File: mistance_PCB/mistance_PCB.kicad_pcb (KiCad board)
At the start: 2 copper layers, 3 parts, among them U1 ESP32-WROOM-32E, U2 TPS61200DRC, U3 MCP73831-2-OT

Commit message: PCB update
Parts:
- added C1: 1uF, Capacitor_SMD:C_1210_3225Metric, F.Cu at (85.3, 44.9)
- added C2: 4.7uF, Capacitor_SMD:C_1210_3225Metric, F.Cu at (85.3, 49.1)
- added C3: 22uF, Capacitor_SMD:C_1210_3225Metric, F.Cu at (85.3, 53.4)
- added C4: 4.7uF, Capacitor_SMD:C_1210_3225Metric, F.Cu at (85.3, 57.6)
- added C5: 4.7uF, Capacitor_SMD:C_1210_3225Metric, F.Cu at (85.3, 61.9)
- added D1: D_Schottky, Diode_SMD:DIOM5226X220N, F.Cu at (93.3, 45.0)
- added J1: USB_B_Micro, Connector_USB:USB_Micro-B_Amphenol_10103594-0001LF_Horizontal, F.Cu at (82.7, 15.6)
- added Q1: Q_PMOS_DSG, SI2333DS-T1-E3:SOT95P237X112-3N, F.Cu at (88.5, 31.0)
- added R1: 2M, Resistor_SMD:R_1210_3225Metric, F.Cu at (95.5, 28.5)
- added R2: 180K, Resistor_SMD:R_1210_3225Metric, F.Cu at (95.5, 22.5)
- added R3: 10K, Resistor_SMD:R_0603_1608Metric, F.Cu at (77.0, 23.3)
- added R4: 10K, Resistor_SMD:R_0603_1608Metric, F.Cu at (82.5, 34.4)
- moved U2 26.8 mm to (104.0, 26.0)
- moved U3 2.44 mm to (78.5, 29.0), turned to 90 degrees
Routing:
- net GND: track 0.00 -> 12.6 mm
- net Net-(J1-D+): track 0.00 -> 0.65 mm

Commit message: PCB update
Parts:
- added BT1: Battery_Cell, Battery:BatteryHolder_MPD_BH-18650-PC2, F.Cu at (87.3, 81.1)
- added C6: 22uF, Capacitor_SMD:C_1210_3225Metric, F.Cu at (72.0, 57.5)
- added C7: 1uF, Capacitor_SMD:C_1210_3225Metric, F.Cu at (72.0, 61.8)
- added C8: 1uF, Capacitor_SMD:C_1210_3225Metric, F.Cu at (72.0, 66.0)
- added L1: 2.2uH, Inductor_SMD:L_1210_3225Metric, F.Cu at (64.6, 57.8)
- added R5: 10K, Resistor_SMD:R_0603_1608Metric, F.Cu at (76.9, 56.6)
- added U4: AMS1117-3.3, Package_TO_SOT_SMD:SOT-223-3_TabPin2, F.Cu at (72.4, 38.7)
- U3: footprint Package_TO_SOT_SMD:SOT-23-5 -> Package_TO_SOT_SMD:SOT95P280X145-5N
- moved R2 53.5 mm to (64.6, 66.2), turned to 0 degrees
- moved J1 50.1 mm to (88.4, 65.3), turned to 90 degrees
- moved R1 45.6 mm to (64.6, 62.0), turned to 0 degrees
- moved U2 41.5 mm to (70.1, 50.0)
- moved R3 25.5 mm to (80.2, 48.6), turned to 0 degrees
- moved Q1 22.5 mm to (75.7, 49.6), turned to 0 degrees
- moved C1 22.3 mm to (64.6, 36.6)
- moved C2 22.3 mm to (64.6, 40.8)
- moved C3 22.3 mm to (64.6, 45.1)
- moved C4 22.3 mm to (64.6, 49.3)
- moved C5 22.3 mm to (64.6, 53.6)
- moved U3 21.3 mm to (84.6, 49.5), turned to 0 degrees
- moved D1 20.7 mm to (72.7, 45.1)
- moved R4 16.9 mm to (80.2, 51.1), turned to 0 degrees
- moved U1 4.27 mm to (36.2, 43.2)
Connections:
- U1 pad 2: unconnected-(U1-VDD-Pad2) -> 3.3V OUT
- U1 pad 3: unconnected-(U1-EN-Pad3) -> Net-(U1-EN)
- U1 pad 34: unconnected-(U1-RXD0/IO3-Pad34) -> RX
- U1 pad 35: unconnected-(U1-TXD0/IO1-Pad35) -> TX
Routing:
- net GND: track 12.6 -> 164.4 mm, vias 0 -> 10
- net 5v OUT: track 0.00 -> 87.8 mm, vias 0 -> 3
- net Net-(BT1-+): track 0.00 -> 81.6 mm, vias 0 -> 1
- net 3.3V OUT: track 0.00 -> 72.1 mm, vias 0 -> 6
- net Net-(U1-EN): track 0.00 -> 69.7 mm, vias 0 -> 5
- net Net-(D1-A): track 0.00 -> 60.2 mm
- net Net-(Q1-D): track 0.00 -> 59.9 mm, vias 0 -> 3
- net Net-(U4-GND): track 0.00 -> 56.3 mm
- net Net-(U2-UVLO): track 0.00 -> 25.4 mm, vias 0 -> 2
- net Net-(U2-VAUX): track 0.00 -> 18.7 mm, vias 0 -> 2
- net Net-(U2-L): track 0.00 -> 13.0 mm, vias 0 -> 2
- net Net-(U3-PROG): track 0.00 -> 7.17 mm

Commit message: PCB update
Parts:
- added C10: 0.1uF, Capacitor_SMD:C_1210_3225Metric, F.Cu at (50.0, 45.8)
- added C11: 1uF, Capacitor_SMD:C_1210_3225Metric, F.Cu at (50.0, 50.0)
- added C9: 0.1uF, Capacitor_SMD:C_1210_3225Metric, F.Cu at (47.8, 64.8)
- added D2: PTVS5V0Z1USK, Diode_SMD:D_01005_0402Metric, F.Cu at (54.2, 44.5)
- added D3: PTVS5V0Z1USK, Diode_SMD:D_01005_0402Metric, F.Cu at (54.2, 46.1)
- added D4: PTVS5V0Z1USK, Diode_SMD:D_01005_0402Metric, F.Cu at (54.2, 47.8)
- added J2: USB_B_Micro, Connector_USB:USB_Micro-B_Amphenol_10103594-0001LF_Horizontal, F.Cu at (88.4, 42.7)
- added L2: 2.2uH, Inductor_SMD:L_1210_3225Metric, F.Cu at (53.4, 64.8)
- added PolarizedCapacitor1: 4.7uF, Capacitor_SMD:C_1210_3225Metric, F.Cu at (50.0, 54.2)
- added PolarizedCapacitor2: 4.7uF, Capacitor_SMD:C_1210_3225Metric, F.Cu at (50.0, 58.5)
- added R6: 22, Resistor_SMD:R_0603_1608Metric, F.Cu at (58.2, 64.0)
- added R7: 22, Resistor_SMD:R_0603_1608Metric, F.Cu at (58.2, 66.5)
- added R8: 4.7K, Resistor_SMD:R_0603_1608Metric, F.Cu at (54.9, 49.8)
- added U5: CP2104, Package_DFN_QFN:QFN-24-1EP_4x4mm_P0.5mm_EP2.6x2.6mm, F.Cu at (57.5, 57.9)
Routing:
- net GND: track 164.4 -> 262.9 mm, vias 10 -> 20
- net Net-(D2-K): track 0.00 -> 79.6 mm, vias 0 -> 6
- net Net-(D3-K): track 0.00 -> 77.0 mm, vias 0 -> 5
- net Net-(D4-K): track 0.00 -> 72.7 mm, vias 0 -> 2
- net 3.3v OUT CP2104: track 0.00 -> 34.6 mm, vias 0 -> 2
- net 3.3V OUT: track 72.1 -> 105.4 mm, vias 6 -> 8
- net USB 5V OUT: track 0.00 -> 29.7 mm, vias 0 -> 2
- net TX: track 0.00 -> 25.7 mm, vias 0 -> 4
- net Net-(U5-VPP): track 0.00 -> 25.5 mm, vias 0 -> 2
- net RX: track 0.00 -> 22.4 mm, vias 0 -> 4
- net Net-(U5-~{RST}): track 0.00 -> 20.6 mm, vias 0 -> 2
- net Net-(U5-D+): track 0.00 -> 11.6 mm
- net Net-(U5-D-): track 0.00 -> 7.75 mm
- net Net-(U1-EN): track 69.7 -> 72.2 mm
- net Net-(D1-A): track 60.2 -> 58.1 mm

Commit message: PCB update
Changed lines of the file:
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@@
 		)
 		(property "Value" "MCP73831-2-OT"
-			(at 13.4146 0.5394 0)
+			(at -0.0854 3.5394 0)
 			(layer "F.Fab")
 			(effects
@@
 		(tags "capacitor")
 		(property "Reference" "PolarizedCapacitor2"
-			(at -9.525 0 0)
+			(at -10.025 0 0)
 			(layer "F.SilkS")
 			(effects
@@
 		(tags "capacitor")
 		(property "Reference" "PolarizedCapacitor1"
-			(at -10.025 -0.25 0)
+			(at -10.025 0.75 0)
 			(layer "F.SilkS")
 			(effects

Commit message: PCB update
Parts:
- added C12: 0.1uF, Capacitor_SMD:C_1210_3225Metric, F.Cu at (13.1, 40.9)
- added C13: PESD0402-140, PESD0402-140:RESC1005X35N, F.Cu at (6.06, 58.0)
- added C14: PESD0402-140, PESD0402-140:RESC1005X35N, F.Cu at (6.06, 56.9)
- added C15: PESD0402-140, PESD0402-140:RESC1005X35N, F.Cu at (6.06, 55.7)
- added C16: PESD0402-140, PESD0402-140:RESC1005X35N, F.Cu at (89.5, 43.6)
- added C17: PESD0402-140, PESD0402-140:RESC1005X35N, F.Cu at (89.5, 45.8)
- added C18: 0.1uF, Capacitor_SMD:C_1210_3225Metric, F.Cu at (18.1, 68.5)
- added C19: 4.7uF, Capacitor_SMD:C_1210_3225Metric, F.Cu at (21.3, 68.5)
- added C20: 27pF, Capacitor_SMD:C_0603_1608Metric, F.Cu at (79.0, 16.0)
- added C21: 12pF, Capacitor_SMD:C_0402_1005Metric, F.Cu at (86.8, 64.7)
- added C22: 12pF, Capacitor_SMD:C_0402_1005Metric, F.Cu at (86.8, 66.6)
- added C23: 0.1uF, Capacitor_SMD:C_1210_3225Metric, F.Cu at (70.1, 61.6)
- added C24: 22uF, Capacitor_SMD:C_1210_3225Metric, F.Cu at (75.7, 36.1)
- added C25: 1uF, Capacitor_SMD:C_1210_3225Metric, F.Cu at (75.7, 40.3)
- added C26: 10uF, Capacitor_SMD:C_1210_3225Metric, F.Cu at (75.7, 44.6)
- added J3: GRPB052VWVN-RC, Varistor:SULLINS_GRPB052VWVN-RC, F.Cu at (14.1, 61.4)
- added J4: OLED, HTSW-104-20-TM-S:SAMTEC_HTSW-104-20-TM-S, F.Cu at (13.7, 71.1)
- added J5: SMA-J-P-X-ST-TH1, SMA-J-P-X-ST-TH1:SAMTEC_SMA-J-P-X-ST-TH1, F.Cu at (84.5, 16.0)
- added L4: WE-TPC_2811, WE-TPC_2811:WE-TPC_2811, F.Cu at (75.5, 16.0)
- added R10: 100R, Resistor_SMD:R_0603_1608Metric, F.Cu at (13.9, 55.3)
- added R11: 100R, Resistor_SMD:R_0603_1608Metric, F.Cu at (13.9, 53.8)
- added R12: 100R, Resistor_SMD:R_0603_1608Metric, F.Cu at (13.9, 52.3)
- added R13: 100R, Resistor_SMD:R_0603_1608Metric, F.Cu at (13.9, 50.8)
- added R14: 2.2K, Resistor_SMD:R_0603_1608Metric, F.Cu at (88.6, 56.2)
- added R15: 2.2K, Resistor_SMD:R_0603_1608Metric, F.Cu at (88.6, 58.7)
- added R9: 100K, Resistor_SMD:R_0603_1608Metric, F.Cu at (17.5, 47.6)
- added S1: SKRPABE010, Diode_SMD:SW_SKRPABE010, F.Cu at (13.3, 37.1)
- added U6: TPS3839DBZ, Package_TO_SOT_SMD:SOT-23, F.Cu at (13.0, 46.7)
- added U7: SX1278, Package_DFN_QFN:QFN-28-1EP_6x6mm_P0.65mm_EP4.8x4.8mm, F.Cu at (76.0, 22.0)
- added Y1: Crystal, Crystal:Crystal_SMD_2012-2Pin_2.0x1.2mm, F.Cu at (87.2, 69.0)
- C8: value 1uF -> PESD0402-140; footprint Capacitor_SMD:C_1210_3225Metric -> PESD0402-140:RESC1005X35N
- moved J2 93.9 mm to (16.5, 103.1), turned to 0 degrees
- moved J1 71.6 mm to (27.5, 103.0), turned to 0 degrees
- moved C8 66.3 mm to (6.06, 59.2), turned to 180 degrees
- moved R5 61.9 mm to (17.8, 38.2)
- moved C6 52.0 mm to (23.2, 39.5)
- moved C7 52.0 mm to (23.2, 43.8)
- moved U2 49.1 mm to (32.9, 82.0)
- moved U5 47.5 mm to (21.1, 88.2)
- moved D4 46.6 mm to (87.7, 80.2)
- moved D2 46.6 mm to (87.7, 76.8)
- moved D3 46.6 mm to (87.7, 78.5)
- moved Q1 44.4 mm to (42.2, 78.7)
- moved U4 42.7 mm to (35.5, 60.2)
- moved U3 40.3 mm to (56.7, 78.6)
- moved C9 36.4 mm to (70.1, 36.1)
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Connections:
- C8 pad 1: Net-(U1-EN) -> Net-(C8-Pad1)
- R5 pad 1: 3.3V OUT -> EN
- R5 pad 2: Net-(U1-EN) -> 3.3V OUT
- U1 pad 11: unconnected-(U1-IO26-Pad11) -> DIO0(IRQ)
- U1 pad 13: unconnected-(U1-IO14-Pad13) -> MTMS
- U1 pad 14: unconnected-(U1-IO12-Pad14) -> MTDI
- U1 pad 16: unconnected-(U1-IO13-Pad16) -> MTCK
- U1 pad 23: unconnected-(U1-IO15-Pad23) -> MTDO
- U1 pad 27: unconnected-(U1-IO16-Pad27) -> RESET
- U1 pad 29: unconnected-(U1-IO5-Pad29) -> SCK
- U1 pad 30: unconnected-(U1-IO18-Pad30) -> NSS(CS)
- U1 pad 31: unconnected-(U1-IO19-Pad31) -> MISO
- U1 pad 33: unconnected-(U1-IO21-Pad33) -> I2C SDL
- U1 pad 36: unconnected-(U1-IO22-Pad36) -> I2C SCL
- U1 pad 37: unconnected-(U1-IO23-Pad37) -> MOSI
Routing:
- net GND: track 262.9 -> 106.2 mm, vias 20 -> 5
- net 5v OUT: track 87.8 -> 0.00 mm, vias 3 -> 0
- net Net-(BT1-+): track 81.6 -> 0.00 mm, vias 1 -> 0
- net Net-(D2-K): track 79.6 -> 0.00 mm, vias 6 -> 0
- net Net-(D3-K): track 77.0 -> 0.00 mm, vias 5 -> 0
- net Net-(D4-K): track 72.7 -> 0.00 mm, vias 2 -> 0
- net Net-(Q1-D): track 59.9 -> 0.00 mm, vias 3 -> 0
- net Net-(D1-A): track 58.1 -> 0.00 mm
- net Net-(U1-EN): track 72.2 -> 23.0 mm, vias 5 -> 2
- net Net-(U4-GND): track 56.3 -> 20.8 mm
- net EN: track 0.00 -> 34.7 mm
- net 3.3v OUT CP2104: track 34.6 -> 0.00 mm, vias 2 -> 0
- net USB 5V OUT: track 29.7 -> 0.00 mm, vias 2 -> 0
- net MTDO: track 0.00 -> 29.7 mm, vias 0 -> 2
- net TX: track 25.7 -> 0.00 mm, vias 4 -> 0
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
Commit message: PCB first chack
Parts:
- moved J2 76.8 mm to (92.4, 91.7), turned to 90 degrees
- moved charger1 68.5 mm to (92.3, 80.7), turned to 90 degrees
- moved R7 65.0 mm to (34.6, 92.7), turned to 180 degrees
- moved R6 56.6 mm to (34.6, 94.2), turned to 180 degrees
- moved U5 50.4 mm to (67.2, 68.1)
- moved C1 44.6 mm to (56.5, 79.9), turned to -90 degrees
- moved R3 44.5 mm to (60.2, 93.2)
- moved C4 42.6 mm to (56.6, 90.7)
- moved Y1 41.9 mm to (83.3, 27.3), turned to -90 degrees
- moved C9 41.7 mm to (63.1, 77.2)
- moved C5 41.0 mm to (64.0, 94.1)
- moved C21 39.2 mm to (79.7, 26.1)
- moved C22 39.2 mm to (79.7, 28.1)
- moved C3 37.1 mm to (53.1, 79.9), turned to -90 degrees
- moved C2 36.6 mm to (53.9, 75.3)
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- renumbered U1 to ESP32, U4 to Regulator1, J1 to charger1
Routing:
- net GND: track 106.2 -> 406.2 mm, vias 5 -> 15
- net 3.3V OUT: track 92.3 -> 184.0 mm, vias 2 -> 6
- net I2C SCL: track 0.00 -> 87.3 mm
- net I2C SDL: track 0.00 -> 83.1 mm, vias 0 -> 4
- net Net-(D3-K): track 0.00 -> 76.5 mm, vias 0 -> 8
- net Net-(D4-K): track 0.00 -> 67.3 mm, vias 0 -> 2
- net Net-(BT1-+): track 0.00 -> 67.1 mm
- net DIO0(IRQ): track 0.00 -> 64.1 mm, vias 0 -> 6
- net Net-(D1-A): track 0.00 -> 61.3 mm, vias 0 -> 4
- net MISO: track 0.00 -> 55.0 mm, vias 0 -> 4
- net SCK: track 0.00 -> 54.8 mm, vias 0 -> 4
- net Net-(Q1-D): track 0.00 -> 53.6 mm, vias 0 -> 2
- net 5v OUT: track 0.00 -> 53.1 mm, vias 0 -> 5
- net MOSI: track 0.00 -> 52.2 mm, vias 0 -> 2
- net NSS(CS): track 0.00 -> 48.7 mm, vias 0 -> 2
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
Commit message: PCB first chack end
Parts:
- U1: renamed from ESP32; footprint RF_Module:ESP32-WROOM-32D -> RF_Module:ESP32-WROOM-32E
- moved J1 7.27 mm to (99.5, 82.0)
- moved J2 7.16 mm to (99.6, 91.7)
- moved U1 3.19 mm to (48.5, 48.3)
- moved J5 0.35 mm to (97.6, 24.7)
- renumbered charger1 to J1, Regulator1 to U4
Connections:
- D1 pad left: (no net) -> Net-(D1-A)
- D1 pad right: (no net) -> 5v OUT
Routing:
- net GND: track 406.2 -> 419.7 mm
- net Net-(D1-A): track 61.3 -> 69.1 mm
- net Net-(D4-K): track 67.3 -> 74.4 mm
- net Net-(D3-K): track 76.5 -> 83.7 mm
- net Net-(D2-K): track 34.8 -> 41.9 mm
- net Net-(J1-D+): track 3.70 -> 5.11 mm
- net USB 5V OUT: track 11.2 -> 10.7 mm
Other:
- board outline added: 86.4 x 99.3 mm

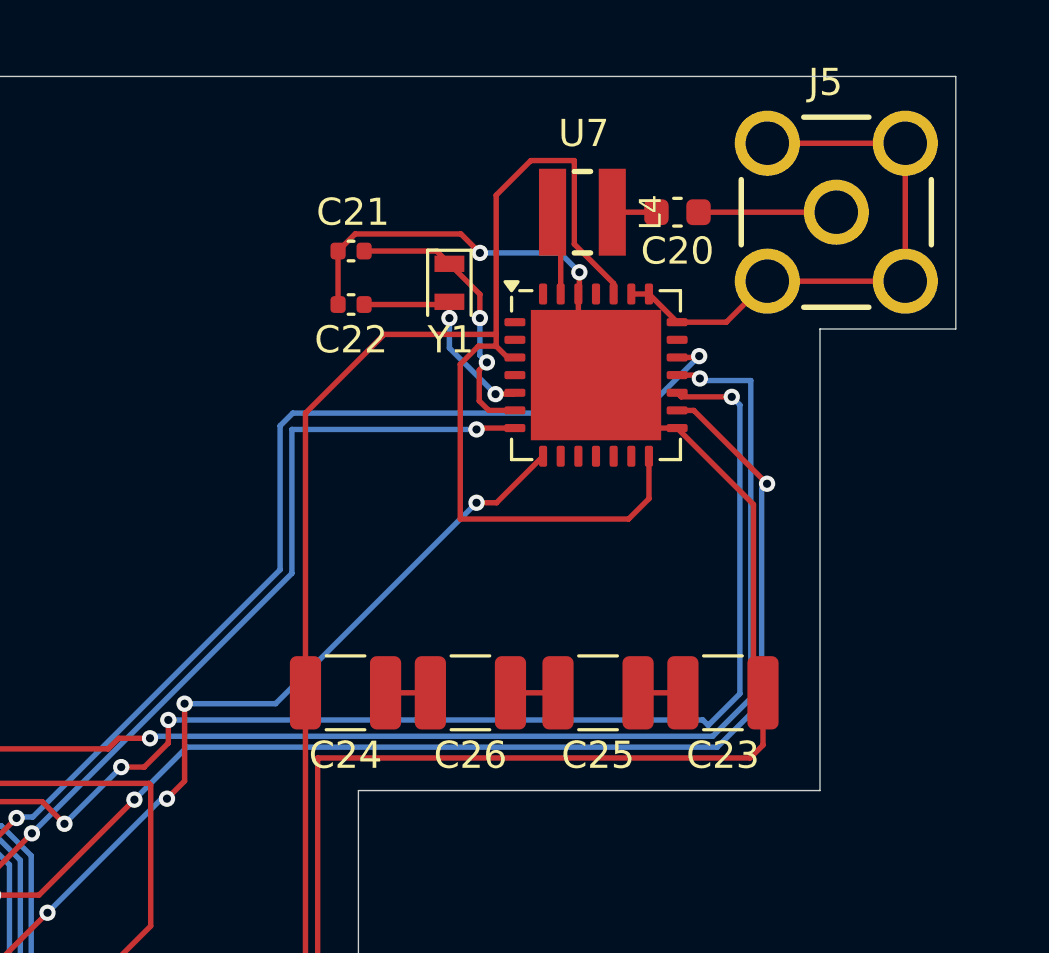
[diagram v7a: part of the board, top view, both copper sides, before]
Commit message: PCB add GND plain
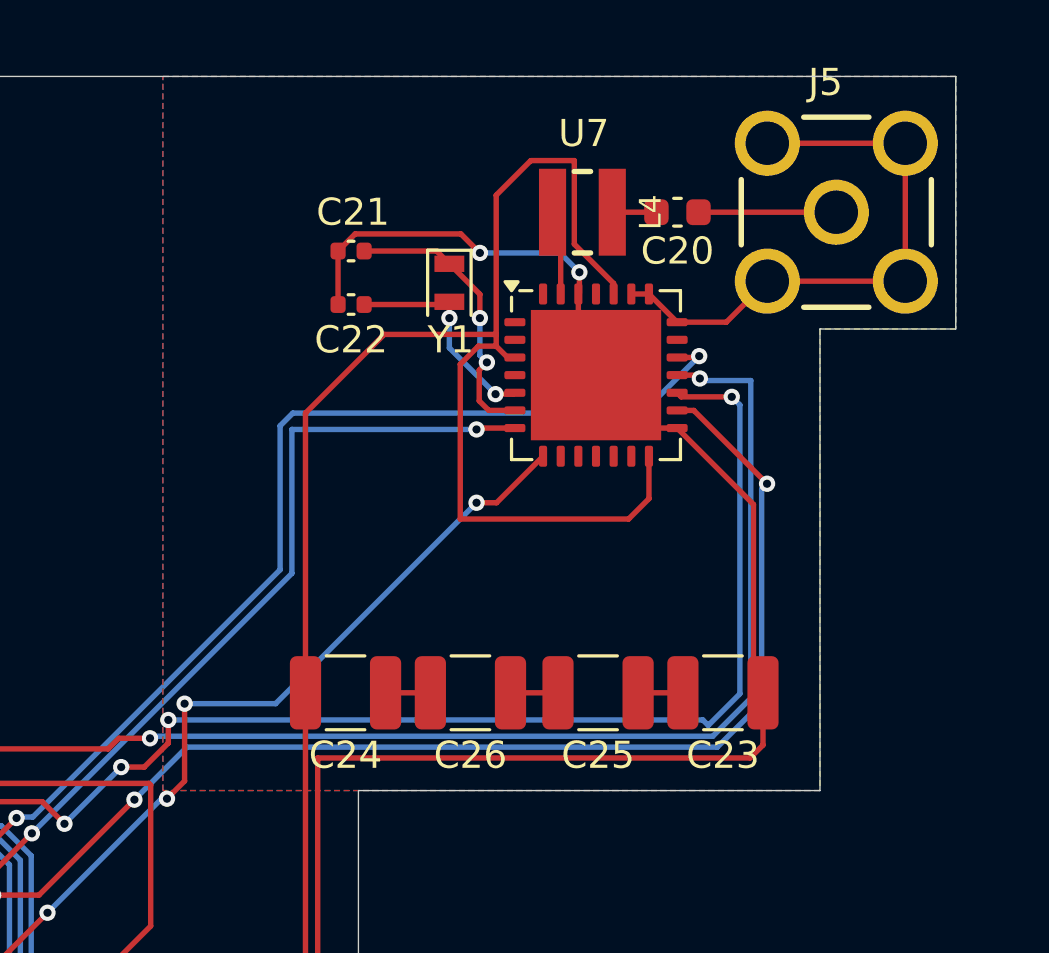
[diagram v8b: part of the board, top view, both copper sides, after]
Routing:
- added copper zone on B.Cu, net GND
- added copper zone on F.Cu, net GND
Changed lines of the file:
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@@
 		(net 77)
+	)
+	(zone
+		(net 18)
+		(net_name "GND")
+		(layers "F.Cu" "B.Cu")
+		(hatch edge 0.5)
+		(connect_pads
+			(clearance 0.5)
+		)
+		(min_thickness 0.25)
+		(filled_areas_thickness no)
+		(fill yes
+			(thermal_gap 0.5)
+			(thermal_bridge_width 0.5)
+		)
+		(polygon
+			(pts
+				(xy 97 46) (xy 72.8 46) (xy 72.8 19.7) (xy 102 19.7) (xy 102 29) (xy 97 29)
+			)
+		)
 	)
 	(embedded_fonts no)
